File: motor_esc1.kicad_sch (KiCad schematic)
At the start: 12 parts, among them U3 MCF8316A

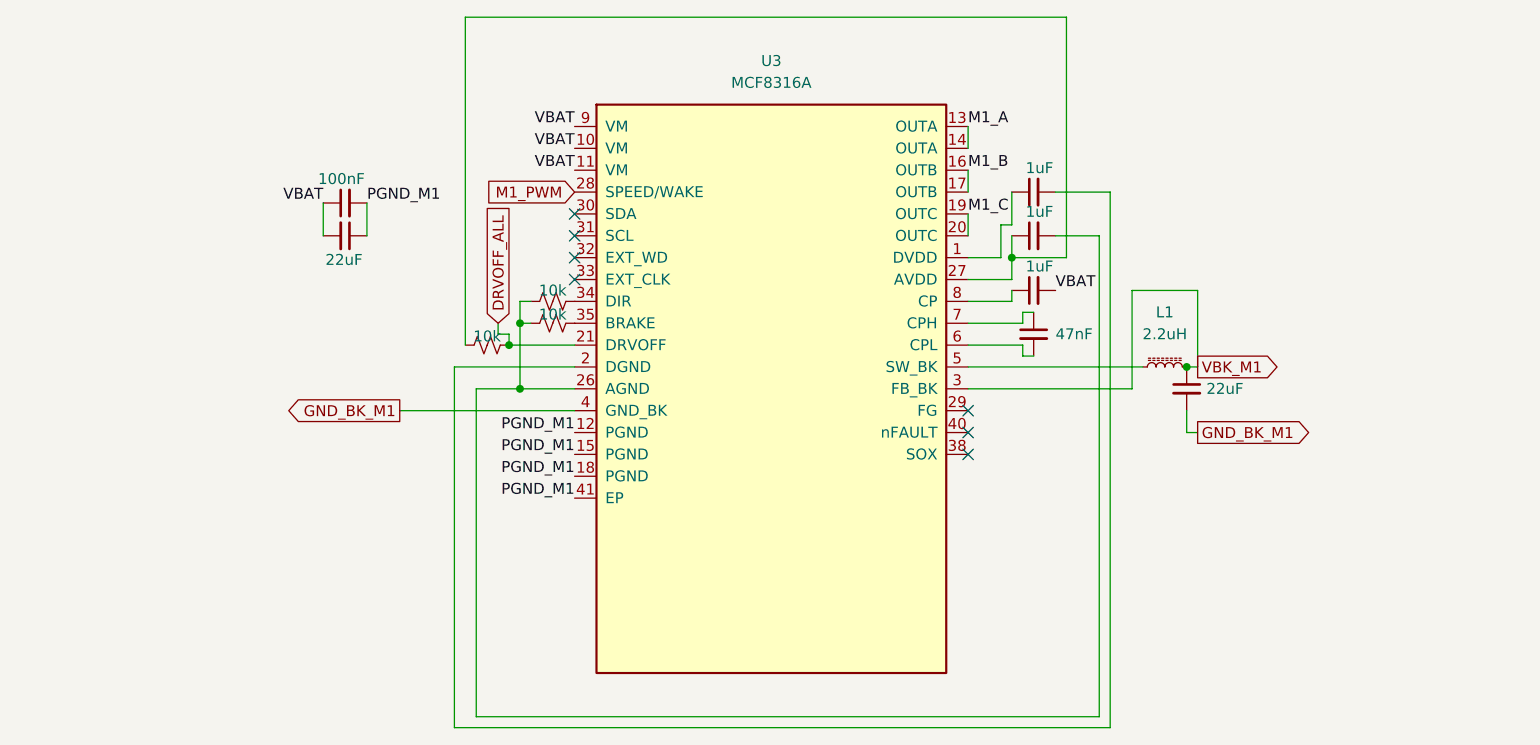
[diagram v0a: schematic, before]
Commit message: A LOT of changes, current state is 2 of 4 ESCs routed, power revamped. \n Board almost done
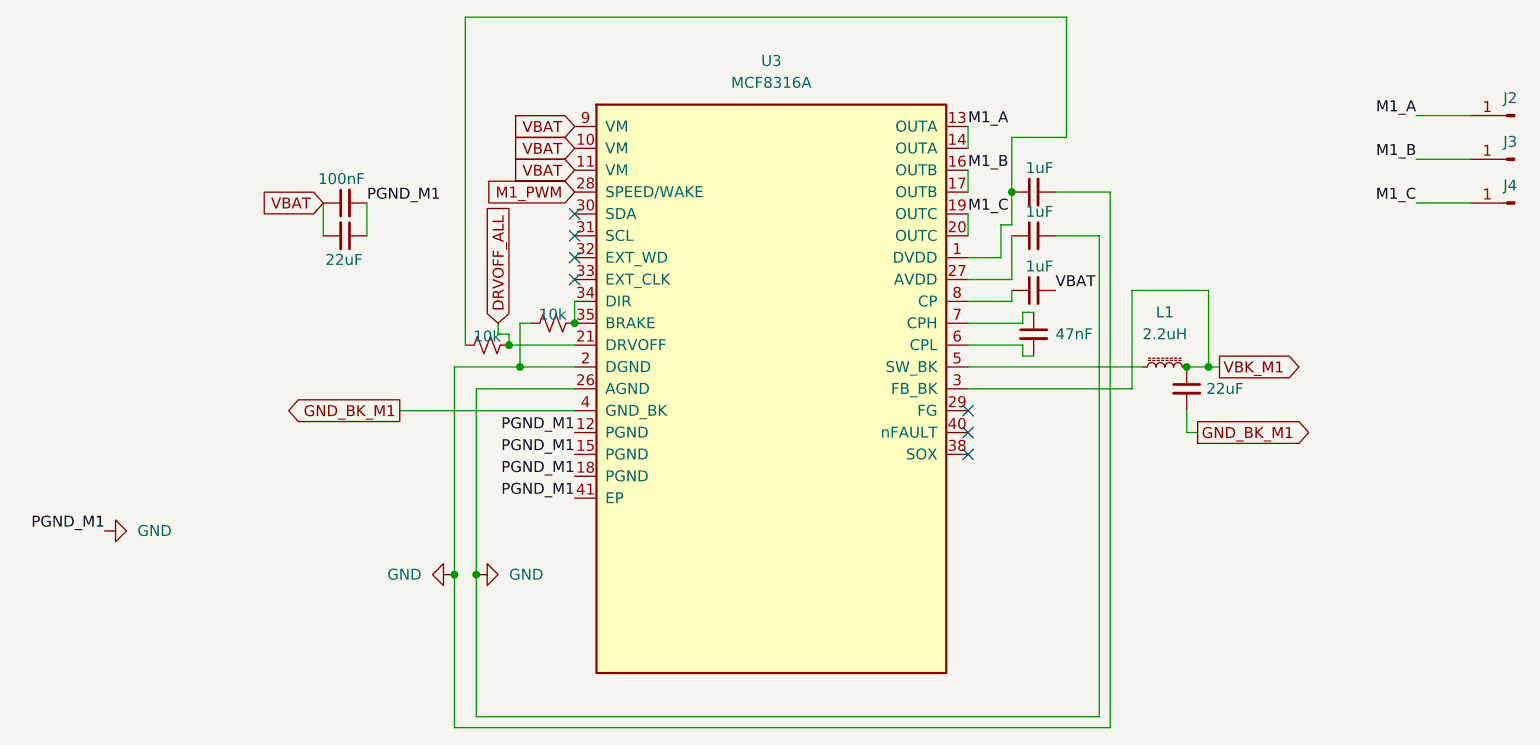
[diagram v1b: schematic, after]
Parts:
- removed R4: 10k, Resistor_SMD:R_0603_1608Metric_Pad0.98x0.95mm_HandSolder, symbol Device:R_Small_US
- added J2, J3, J4: SolderWirePad_1x01_SMD_3x6mm, Connector_Wire:SolderWirePad_1x01_SMD_3x6mm, symbol Connector:Conn_01x01_Pin
- U3: footprint MCF8316:MCF8316A_RGF0040E_VQFN-40-1EP_7x5mm_P0.5mm_EP5.5x3.5mm_kicad5_fixed_rotation -> MCF8316:MCF8316A_RGF0040E_VQFN-40-1EP_7x5mm_P0.5mm_EP5.5x3.5mm
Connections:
- net PGND_M1 is gone; now on net GND: C10.1, C11.2, U3.12 (PGND), U3.15 (PGND), U3.18 (PGND), U3.41 (EP)
- net M1_A: now also J2.1 (Pin_1)
- net M1_B: now also J3.1 (Pin_1)
- net M1_C: now also J4.1 (Pin_1)
- net at C14.1, U3.27 (AVDD): no longer R6.1
- net at C15.1, U3.1 (DVDD): now also R6.1
- net GND: now reaches C15.2, U3.2 (DGND)
- net GND: now also C14.2, R5.1, U3.26 (AGND)
- net at U3.34 (DIR): now also R5.2, U3.35 (BRAKE)

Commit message: done?
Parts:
- removed R6: 10k, Resistor_SMD:R_0603_1608Metric_Pad0.98x0.95mm_HandSolder, symbol Device:R_Small_US
- R5: footprint Resistor_SMD:R_0603_1608Metric_Pad0.98x0.95mm_HandSolder -> Resistor_SMD:R_0402_1005Metric_Pad0.72x0.64mm_HandSolder
